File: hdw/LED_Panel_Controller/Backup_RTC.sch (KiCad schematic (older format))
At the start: 14 parts

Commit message: made a lot more schematic progress
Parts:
- removed C? (x3): 0.1uF, symbol Custom_Library:C_Custom
- removed C?: 10uF, symbol Custom_Library:C_Custom
- removed R?: 1.07M, Resistors_SMD:R_0402, symbol Custom_Library:R_Custom
- added C? (x3): 0.1uF, symbol Custom_Library:C_Custom
- added C?: 10uF, symbol Custom_Library:C_Custom
- added R?: 1.07M, Resistors_SMD:R_0402, symbol Custom_Library:R_Custom
- BT? (x2), C?, R?, U? (x2): Configuration (none) -> BACKUP_RTC
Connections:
- net +3V3: now also C?.1, C?.1
- net GND: now also C?.2, C?.2, C?.2, C?.2
- net VBAT: now also C?.1, C?.1, R?.1
- net VBAT_ADC: now also R?.2
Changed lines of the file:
@@
 F 3 "http://datasheets.maximintegrated.com/en/ds/DS3231M.pdf" H 5050 1400 50  0001 C CNN
 F 4 "DS3231MZ+-ND" H 5050 2000 50  0001 C CNN "Digi-Key PN"
+F 5 "BACKUP_RTC" H 5050 1370 50  0000 C CNN "Configuration"
 	1    5050 2000
 	1    0    0    -1
@@
 I2C_SCL
 $Comp
-L Custom_Library:C_Custom C?
-U 1 1 5E21E9AC
-P 5470 3190
-F 0 "C?" H 5495 3290 50  0000 L CNN
-F 1 "0.1uF" H 5495 3090 50  0000 L CNN
-F 2 "" H 5508 3040 50  0001 C CNN
-F 3 "" H 5495 3290 50  0001 C CNN
-F 4 "0402" H 5320 3290 50  0000 R CNN "display_footprint"
-F 5 "50V" H 5320 3190 50  0000 R CNN "Voltage"
-F 6 "X7R" H 5320 3090 50  0000 R CNN "Dielectric"
-F 7 "" H 5470 3190 50  0001 C CNN "Digi-Key PN"
-	1    5470 3190
-	1    0    0    -1
-$EndComp
-$Comp
 L power:+3.3V #PWR?
 U 1 1 5E21E9B2
-P 5470 3040
-F 0 "#PWR?" H 5470 2890 50  0001 C CNN
-F 1 "+3.3V" H 5470 3180 50  0000 C CNN
-F 2 "" H 5470 3040 50  0000 C CNN
-F 3 "" H 5470 3040 50  0000 C CNN
-	1    5470 3040
+P 5850 3040
+F 0 "#PWR?" H 5850 2890 50  0001 C CNN
+F 1 "+3.3V" H 5850 3180 50  0000 C CNN
+F 2 "" H 5850 3040 50  0000 C CNN
+F 3 "" H 5850 3040 50  0000 C CNN
+	1    5850 3040
 	1    0    0    -1
 $EndComp
@@
 L power:GND #PWR?
 U 1 1 5E21E9B8
-P 5470 3340
-F 0 "#PWR?" H 5470 3090 50  0001 C CNN
-F 1 "GND" H 5470 3190 50  0000 C CNN
-F 2 "" H 5470 3340 50  0001 C CNN
-F 3 "" H 5470 3340 50  0001 C CNN
-	1    5470 3340
-	1    0    0    -1
-$EndComp
-$Comp
-L Custom_Library:C_Custom C?
-U 1 1 5E220EDC
-P 4740 3190
-F 0 "C?" H 4765 3290 50  0000 L CNN
-F 1 "0.1uF" H 4765 3090 50  0000 L CNN
-F 2 "" H 4778 3040 50  0001 C CNN
-F 3 "" H 4765 3290 50  0001 C CNN
-F 4 "0402" H 4590 3290 50  0000 R CNN "display_footprint"
-F 5 "50V" H 4590 3190 50  0000 R CNN "Voltage"
-F 6 "X7R" H 4590 3090 50  0000 R CNN "Dielectric"
-F 7 "" H 4740 3190 50  0001 C CNN "Digi-Key PN"
-	1    4740 3190
+P 5850 3340
+F 0 "#PWR?" H 5850 3090 50  0001 C CNN
+F 1 "GND" H 5850 3190 50  0000 C CNN
+F 2 "" H 5850 3340 50  0001 C CNN
+F 3 "" H 5850 3340 50  0001 C CNN
+	1    5850 3340
 	1    0    0    -1
 $EndComp
@@
 F 3 "~" V 1140 4820 50  0001 C CNN
 F 4 "P034-ND" H 1140 4760 50  0001 C CNN "Digi-Key PN"
+F 5 "BACKUP_RTC" H 790 4760 50  0000 C CNN "Configuration"
 	1    1140 4760
 	1    0    0    -1
@@
 F 3 "~" V 1880 4820 50  0001 C CNN
 F 4 "BU1632SM-JJ-GCT-ND" H 1880 4760 50  0001 C CNN "Digi-Key PN"
+F 5 "BACKUP_RTC" H 2220 4670 50  0000 C CNN "Configuration"
 	1    1880 4760
 	1    0    0    -1
@@
 F 3 "http://www.ti.com/lit/ds/symlink/tlv6700.pdf" H 5330 4870 60  0001 C CNN
 F 4 "296-51696-1-ND" H 5330 4870 50  0001 C CNN "Digi-Key PN"
+F 5 "BACKUP_RTC" H 5330 4030 50  0000 C CNN "Configuration"
 	1    5330 4870
 	1    0    0    -1
@@
 L power:GND #PWR?
 U 1 1 5F2CCEAA
-P 3950 3340
-F 0 "#PWR?" H 3950 3090 50  0001 C CNN
-F 1 "GND" H 3950 3190 50  0000 C CNN
-F 2 "" H 3950 3340 50  0001 C CNN
-F 3 "" H 3950 3340 50  0001 C CNN
-	1    3950 3340
-	1    0    0    -1
-$EndComp
-$Comp
-L Custom_Library:C_Custom C?
-U 1 1 5F2CCEB4
-P 3950 3190
-AR Path="/5CB7718D/5F2CCEB4" Ref="C?"  Part="1"
-AR Path="/5E0DC082/5F2CCEB4" Ref="C?"  Part="1"
-AR Path="/5E0F9110/5F2CCEB4" Ref="C?"  Part="1"
-AR Path="/5A557C58/5F2CCEB4" Ref="C?"  Part="1"
-AR Path="/5CB25152/5F2CCEB4" Ref="C?"  Part="1"
-AR Path="/5E697934/5F2CCEB4" Ref="C?"  Part="1"
-AR Path="/5EAE2F02/5F2CCEB4" Ref="C?"  Part="1"
-AR Path="/5EAE3021/5F2CCEB4" Ref="C?"  Part="1"
-AR Path="/5EAE2D8A/5F2CCEB4" Ref="C?"  Part="1"
-AR Path="/5E939D31/5F2CCEB4" Ref="C?"  Part="1"
-AR Path="/5E939EED/5F2CCEB4" Ref="C?"  Part="1"
-AR Path="/5F582E7C/5F2CCEB4" Ref="C?"  Part="1"
-F 0 "C?" H 3975 3290 50  0000 L CNN
-F 1 "10uF" H 3975 3090 50  0000 L CNN
-F 2 "" H 3988 3040 50  0001 C CNN
-F 3 "" H 3975 3290 50  0001 C CNN
-F 4 "0402" H 3800 3290 50  0000 R CNN "display_footprint"
-F 5 "10V" H 3800 3190 50  0000 R CNN "Voltage"
-F 6 "X5R" H 3800 3090 50  0000 R CNN "Dielectric"
-F 7 "1276-6830-1-ND" H 3950 3190 50  0001 C CNN "Digi-Key PN"
-	1    3950 3190
+P 3580 3340
+F 0 "#PWR?" H 3580 3090 50  0001 C CNN
+F 1 "GND" H 3580 3190 50  0000 C CNN
+F 2 "" H 3580 3340 50  0001 C CNN
+F 3 "" H 3580 3340 50  0001 C CNN
+	1    3580 3340
 	1    0    0    -1
 $EndComp
@@
 L Custom_Library:VBAT #PWR?
 U 1 1 5F2CCEF3
-P 3950 3040
-F 0 "#PWR?" H 3950 2890 50  0001 C CNN
-F 1 "VBAT" H 3950 3190 50  0000 C CNN
-F 2 "" H 3950 3040 50  0001 C CNN
-F 3 "" H 3950 3040 50  0001 C CNN
-	1    3950 3040
-	1    0    0    -1
-$EndComp
-$Comp
-L Custom_Library:C_Custom C?
-U 1 1 5F3B2874
-P 5990 5960
-F 0 "C?" H 6015 6060 50  0000 L CNN
-F 1 "0.1uF" H 6015 5860 50  0000 L CNN
-F 2 "" H 6028 5810 50  0001 C CNN
-F 3 "" H 6015 6060 50  0001 C CNN
-F 4 "0402" H 5840 6060 50  0000 R CNN "display_footprint"
-F 5 "50V" H 5840 5960 50  0000 R CNN "Voltage"
-F 6 "X7R" H 5840 5860 50  0000 R CNN "Dielectric"
-F 7 "" H 5990 5960 50  0001 C CNN "Digi-Key PN"
-	1    5990 5960
+P 3580 3040
+F 0 "#PWR?" H 3580 2890 50  0001 C CNN
+F 1 "VBAT" H 3580 3190 50  0000 C CNN
+F 2 "" H 3580 3040 50  0001 C CNN
+F 3 "" H 3580 3040 50  0001 C CNN
+	1    3580 3040
 	1    0    0    -1
 $EndComp
@@
 F 5 "50V" H 3150 4850 50  0000 R CNN "Voltage"
 F 6 "X7R" H 3150 4750 50  0000 R CNN "Dielectric"
-F 7 "" H 3300 4850 50  0001 C CNN "Digi-Key PN"
+F 7 "BACKUP_RTC" H 3680 4850 50  0000 C CNN "Configuration"
 	1    3300 4850
 	-1   0    0    -1
@@
 	1    2150 4090
 	1    0    0    -1
-$EndComp
-$Comp
-L Custom_Library:R_Custom R?
-U 1 1 5F39B3AD
-P 4130 4390
-AR Path="/5BB27BA3/5F39B3AD" Ref="R?"  Part="1"
-AR Path="/5BB27BF7/5F39B3AD" Ref="R?"  Part="1"
-AR Path="/5C1DE17A/5F39B3AD" Ref="R?"  Part="1"
-AR Path="/5C1E3A08/5F39B3AD" Ref="R?"  Part="1"
-AR Path="/5D779AE1/5F39B3AD" Ref="R?"  Part="1"
-AR Path="/5CB7718D/5F39B3AD" Ref="R?"  Part="1"
-AR Path="/5E0DC082/5F39B3AD" Ref="R?"  Part="1"
-AR Path="/5E0F263A/5F39B3AD" Ref="R?"  Part="1"
-AR Path="/5A557C58/5F39B3AD" Ref="R?"  Part="1"
-AR Path="/5E2843EF/5F39B3AD" Ref="R?"  Part="1"
-AR Path="/5F360CB6/5F39B3AD" Ref="R?"  Part="1"
-AR Path="/5E939EED/5F39B3AD" Ref="R?"  Part="1"
-AR Path="/5F582E7C/5F39B3AD" Ref="R?"  Part="1"
-F 0 "R?" H 4050 4390 50  0000 R CNN
-F 1 "1.07M" V 4130 4390 40  0000 C CNN
-F 2 "Resistors_SMD:R_0402" H 4130 4390 50  0001 C CNN
-F 3 "" H 4130 4390 50  0001 C CNN
-F 4 "0402" H 4230 4470 50  0000 L CNN "display_footprint"
-F 5 "1%" H 4230 4390 50  0000 L CNN "Tolerance"
-F 6 "1/16W" H 4240 4310 50  0000 L CNN "Wattage"
-F 7 "" H 4130 4390 50  0001 C CNN "Digi-Key PN"
-	1    4130 4390
-	-1   0    0    -1
 $EndComp
 $Comp
@@
 F 5 "1%" H 4230 4850 50  0000 L CNN "Tolerance"
 F 6 "1/16W" H 4240 4770 50  0000 L CNN "Wattage"
-F 7 "" H 4130 4850 50  0001 C CNN "Digi-Key PN"
+F 7 "BACKUP_RTC" H 4090 5010 50  0000 R CNN "Configuration"
 	1    4130 4850
 	-1   0    0    -1
@@
 Connection ~ 3300 4620
 NoConn ~ 5550 1800
+$Comp
+L Custom_Library:R_Custom R?
+U 1 1 6021E2B7
+P 4130 4390
+AR Path="/5BB27BA3/6021E2B7" Ref="R?"  Part="1"
+AR Path="/5BB27BF7/6021E2B7" Ref="R?"  Part="1"
+AR Path="/5C1DE17A/6021E2B7" Ref="R?"  Part="1"
+AR Path="/5C1E3A08/6021E2B7" Ref="R?"  Part="1"
+AR Path="/5D779AE1/6021E2B7" Ref="R?"  Part="1"
+AR Path="/5CB7718D/6021E2B7" Ref="R?"  Part="1"
+AR Path="/5E0DC082/6021E2B7" Ref="R?"  Part="1"
+AR Path="/5E0F263A/6021E2B7" Ref="R?"  Part="1"
+AR Path="/5A557C58/6021E2B7" Ref="R?"  Part="1"
+AR Path="/5E2843EF/6021E2B7" Ref="R?"  Part="1"
+AR Path="/5F360CB6/6021E2B7" Ref="R?"  Part="1"
+AR Path="/5E939EED/6021E2B7" Ref="R?"  Part="1"
+AR Path="/5F582E7C/6021E2B7" Ref="R?"  Part="1"
+F 0 "R?" H 4050 4390 50  0000 R CNN
+F 1 "1.07M" V 4130 4390 40  0000 C CNN
+F 2 "Resistors_SMD:R_0402" H 4130 4390 50  0001 C CNN
+F 3 "" H 4130 4390 50  0001 C CNN
+F 4 "0402" H 4230 4470 50  0000 L CNN "display_footprint"
+F 5 "1%" H 4230 4390 50  0000 L CNN "Tolerance"
+F 6 "1/16W" H 4240 4310 50  0000 L CNN "Wattage"
+F 7 "BACKUP_RTC" H 4090 4550 50  0000 R CNN "Configuration"
+	1    4130 4390
+	-1   0    0    -1
+$EndComp
+$Comp
+L Custom_Library:C_Custom C?
+U 1 1 602245D4
+P 5990 5960
+F 0 "C?" H 6015 6060 50  0000 L CNN
+F 1 "0.1uF" H 6015 5860 50  0000 L CNN
+F 2 "" H 6028 5810 50  0001 C CNN
+F 3 "" H 6015 6060 50  0001 C CNN
+F 4 "0402" H 5840 6060 50  0000 R CNN "display_footprint"
+F 5 "50V" H 5840 5960 50  0000 R CNN "Voltage"
+F 6 "X7R" H 5840 5860 50  0000 R CNN "Dielectric"
+F 7 "BACKUP_RTC" H 6370 5960 50  0000 C CNN "Configuration"
+	1    5990 5960
+	-1   0    0    -1
+$EndComp
+$Comp
+L Custom_Library:C_Custom C?
+U 1 1 6022626F
+P 5850 3190
+F 0 "C?" H 5875 3290 50  0000 L CNN
+F 1 "0.1uF" H 5875 3090 50  0000 L CNN
+F 2 "" H 5888 3040 50  0001 C CNN
+F 3 "" H 5875 3290 50  0001 C CNN
+F 4 "0402" H 5700 3290 50  0000 R CNN "display_footprint"
+F 5 "50V" H 5700 3190 50  0000 R CNN "Voltage"
+F 6 "X7R" H 5700 3090 50  0000 R CNN "Dielectric"
+F 7 "BACKUP_RTC" H 6230 3190 50  0000 C CNN "Configuration"
+	1    5850 3190
+	-1   0    0    -1
+$EndComp
+$Comp
+L Custom_Library:C_Custom C?
+U 1 1 602278F5
+P 4740 3190
+F 0 "C?" H 4765 3290 50  0000 L CNN
+F 1 "0.1uF" H 4765 3090 50  0000 L CNN
+F 2 "" H 4778 3040 50  0001 C CNN
+F 3 "" H 4765 3290 50  0001 C CNN
+F 4 "0402" H 4590 3290 50  0000 R CNN "display_footprint"
+F 5 "50V" H 4590 3190 50  0000 R CNN "Voltage"
+F 6 "X7R" H 4590 3090 50  0000 R CNN "Dielectric"
+F 7 "BACKUP_RTC" H 5120 3190 50  0000 C CNN "Configuration"
+	1    4740 3190
+	-1   0    0    -1
+$EndComp
+$Comp
+L Custom_Library:C_Custom C?
+U 1 1 6022C07C
+P 3580 3190
+F 0 "C?" H 3605 3290 50  0000 L CNN
+F 1 "10uF" H 3605 3090 50  0000 L CNN
+F 2 "" H 3618 3040 50  0001 C CNN
+F 3 "" H 3605 3290 50  0001 C CNN
+F 4 "0402" H 3430 3290 50  0000 R CNN "display_footprint"
+F 5 "10V" H 3430 3190 50  0000 R CNN "Voltage"
+F 6 "X7R" H 3430 3090 50  0000 R CNN "Dielectric"
+F 7 "BACKUP_RTC" H 3960 3190 50  0000 C CNN "Configuration"
+	1    3580 3190
+	-1   0    0    -1
+$EndComp
 $EndSCHEMATC

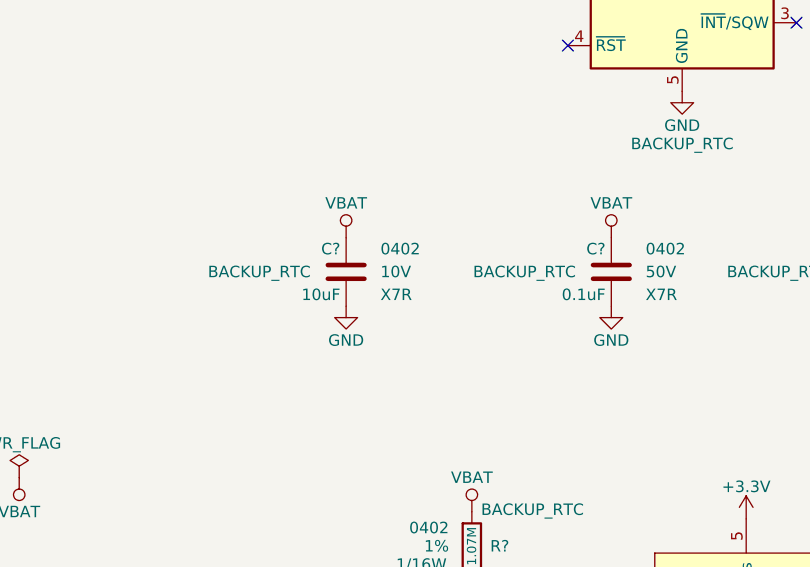
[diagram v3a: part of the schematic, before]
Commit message: added digikey pns, footprints, bom scrubbed
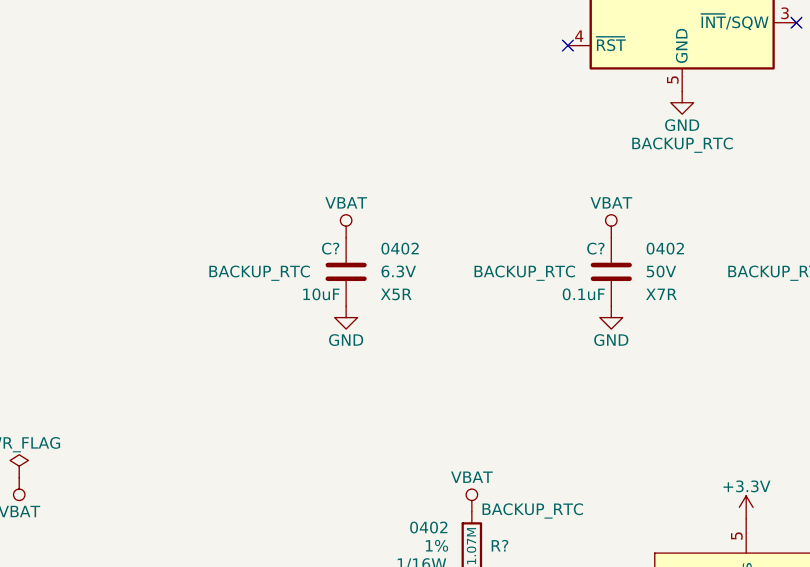
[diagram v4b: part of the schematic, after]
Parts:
- C? (x4): footprint (none) -> Capacitors_SMD:C_0402; Digi-Key PN (none) -> 490-10701-1-ND
- C?: footprint (none) -> Capacitors_SMD:C_0402; Dielectric X7R -> X5R; Digi-Key PN (none) -> 1276-1451-1-ND; Voltage 10V -> 6.3V
- R?: Digi-Key PN (none) -> RMCF0402FT10K0CT-ND
- R?: Digi-Key PN (none) -> RMCF0402FT220KCT-ND
- R?: Digi-Key PN (none) -> RMCF0402FT1M07CT-ND
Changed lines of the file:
@@
 F 5 "1%" H 6280 4390 50  0000 L CNN "Tolerance"
 F 6 "1/16W" H 6280 4320 50  0000 L CNN "Wattage"
-F 7 "" H 6210 4390 50  0001 C CNN "Digi-Key PN"
+F 7 "RMCF0402FT10K0CT-ND" H 6210 4390 50  0001 C CNN "Digi-Key PN"
 	1    6210 4390
 	-1   0    0    -1
@@
 F 0 "C?" H 3325 4950 50  0000 L CNN
 F 1 "0.1uF" H 3325 4750 50  0000 L CNN
-F 2 "" H 3338 4700 50  0001 C CNN
+F 2 "Capacitors_SMD:C_0402" H 3338 4700 50  0001 C CNN
 F 3 "" H 3325 4950 50  0001 C CNN
 F 4 "0402" H 3150 4950 50  0000 R CNN "display_footprint"
@@
 F 6 "X7R" H 3150 4750 50  0000 R CNN "Dielectric"
 F 7 "BACKUP_RTC" H 3680 4850 50  0000 C CNN "Configuration"
+F 8 "490-10701-1-ND" H 3300 4850 50  0001 C CNN "Digi-Key PN"
 	1    3300 4850
 	-1   0    0    -1
@@
 F 6 "1/16W" H 4240 4770 50  0000 L CNN "Wattage"
 F 7 "BACKUP_RTC" H 4090 5010 50  0000 R CNN "Configuration"
+F 8 "RMCF0402FT220KCT-ND" H 4130 4850 50  0001 C CNN "Digi-Key PN"
 	1    4130 4850
 	-1   0    0    -1
@@
 F 6 "1/16W" H 4240 4310 50  0000 L CNN "Wattage"
 F 7 "BACKUP_RTC" H 4090 4550 50  0000 R CNN "Configuration"
+F 8 "RMCF0402FT1M07CT-ND" H 4130 4390 50  0001 C CNN "Digi-Key PN"
 	1    4130 4390
 	-1   0    0    -1
@@
 F 0 "C?" H 6015 6060 50  0000 L CNN
 F 1 "0.1uF" H 6015 5860 50  0000 L CNN
-F 2 "" H 6028 5810 50  0001 C CNN
+F 2 "Capacitors_SMD:C_0402" H 6028 5810 50  0001 C CNN
 F 3 "" H 6015 6060 50  0001 C CNN
 F 4 "0402" H 5840 6060 50  0000 R CNN "display_footprint"
@@
 F 6 "X7R" H 5840 5860 50  0000 R CNN "Dielectric"
 F 7 "BACKUP_RTC" H 6370 5960 50  0000 C CNN "Configuration"
+F 8 "490-10701-1-ND" H 5990 5960 50  0001 C CNN "Digi-Key PN"
 	1    5990 5960
 	-1   0    0    -1
@@
 F 0 "C?" H 5875 3290 50  0000 L CNN
 F 1 "0.1uF" H 5875 3090 50  0000 L CNN
-F 2 "" H 5888 3040 50  0001 C CNN
+F 2 "Capacitors_SMD:C_0402" H 5888 3040 50  0001 C CNN
 F 3 "" H 5875 3290 50  0001 C CNN
 F 4 "0402" H 5700 3290 50  0000 R CNN "display_footprint"
@@
 F 6 "X7R" H 5700 3090 50  0000 R CNN "Dielectric"
 F 7 "BACKUP_RTC" H 6230 3190 50  0000 C CNN "Configuration"
+F 8 "490-10701-1-ND" H 5850 3190 50  0001 C CNN "Digi-Key PN"
 	1    5850 3190
 	-1   0    0    -1
@@
 F 0 "C?" H 4765 3290 50  0000 L CNN
 F 1 "0.1uF" H 4765 3090 50  0000 L CNN
-F 2 "" H 4778 3040 50  0001 C CNN
+F 2 "Capacitors_SMD:C_0402" H 4778 3040 50  0001 C CNN
 F 3 "" H 4765 3290 50  0001 C CNN
 F 4 "0402" H 4590 3290 50  0000 R CNN "display_footprint"
@@
 F 6 "X7R" H 4590 3090 50  0000 R CNN "Dielectric"
 F 7 "BACKUP_RTC" H 5120 3190 50  0000 C CNN "Configuration"
+F 8 "490-10701-1-ND" H 4740 3190 50  0001 C CNN "Digi-Key PN"
 	1    4740 3190
 	-1   0    0    -1
@@
 F 0 "C?" H 3605 3290 50  0000 L CNN
 F 1 "10uF" H 3605 3090 50  0000 L CNN
-F 2 "" H 3618 3040 50  0001 C CNN
+F 2 "Capacitors_SMD:C_0402" H 3618 3040 50  0001 C CNN
 F 3 "" H 3605 3290 50  0001 C CNN
 F 4 "0402" H 3430 3290 50  0000 R CNN "display_footprint"
-F 5 "10V" H 3430 3190 50  0000 R CNN "Voltage"
-F 6 "X7R" H 3430 3090 50  0000 R CNN "Dielectric"
+F 5 "6.3V" H 3430 3190 50  0000 R CNN "Voltage"
+F 6 "X5R" H 3430 3090 50  0000 R CNN "Dielectric"
 F 7 "BACKUP_RTC" H 3960 3190 50  0000 C CNN "Configuration"
+F 8 "1276-1451-1-ND" H 3580 3190 50  0001 C CNN "Digi-Key PN"
 	1    3580 3190
 	-1   0    0    -1
